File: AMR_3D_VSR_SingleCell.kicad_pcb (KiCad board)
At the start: 2 copper layers, 200.8 x 132.1 mm, 32 parts, among them P1 CONN_01X01, P2 CONN_01X01, P3 CONN_02X15, P4 CONN_02X05, P5 CONN_02X02, U1 AFF755b, U10 AFF755b, U11 AFF755b, U12 AFF755b, U13 AFF755b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

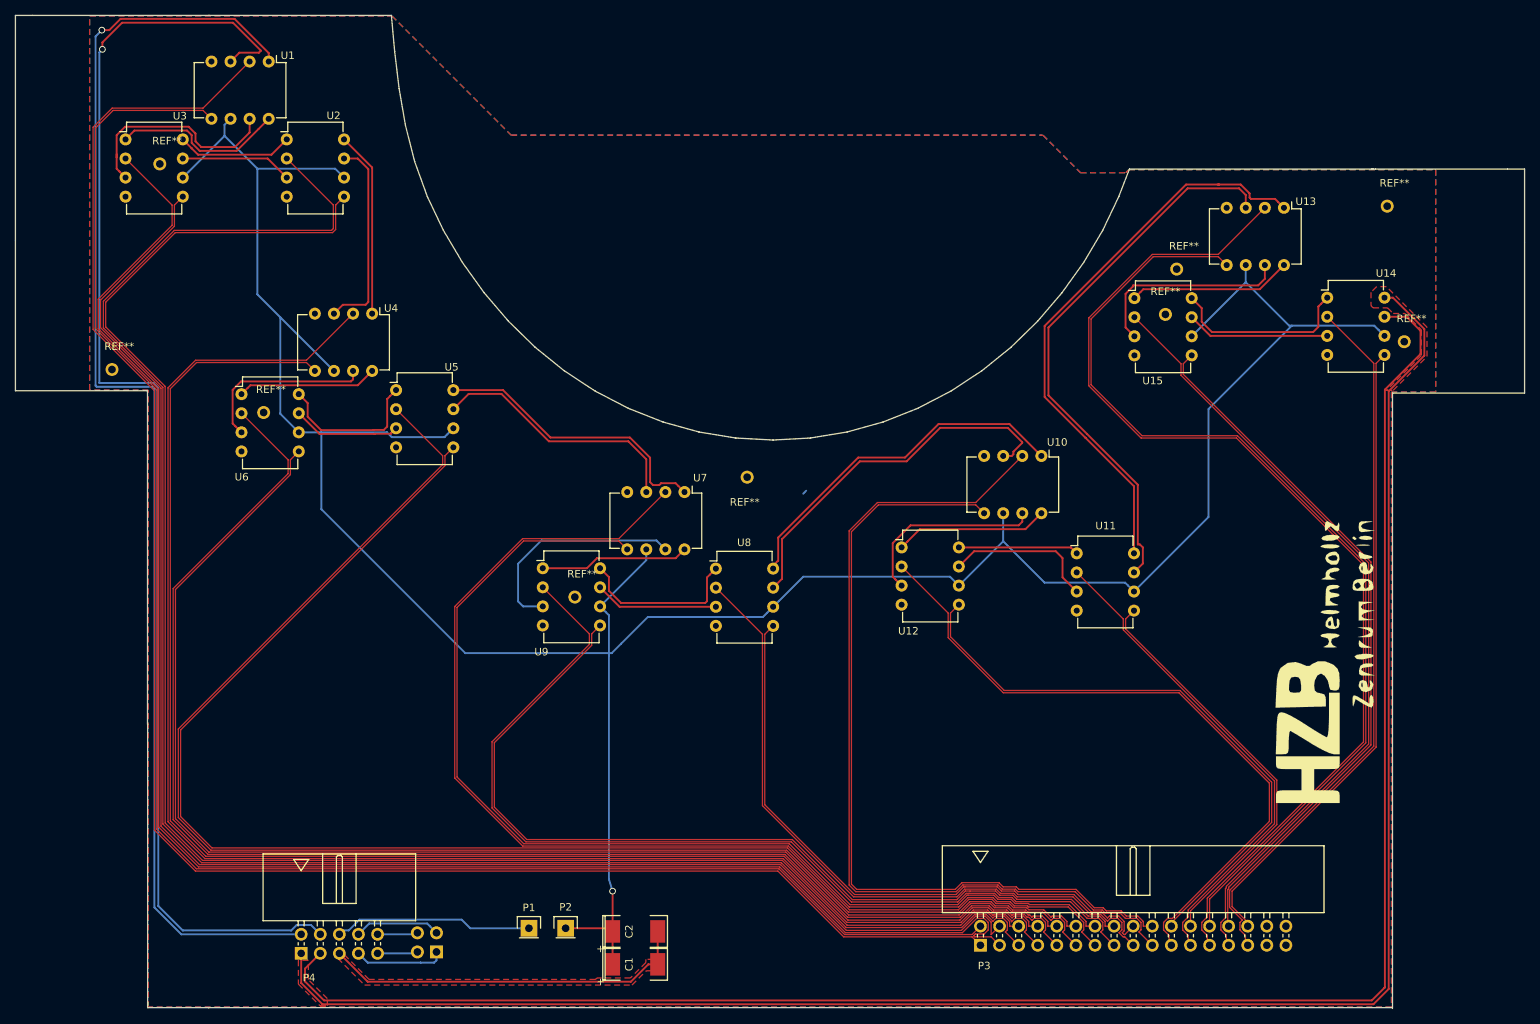
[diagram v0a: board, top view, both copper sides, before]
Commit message: Drillholes + additional load included.  Committer: Schmitz <ltu@basisit.de>  Changes to be committed: 	modified:   AMR_3D_VSR_SingleCell.kicad_pcb 	modified:   AMR_3D_VSR_SingleCell.kicad_pcb-bak
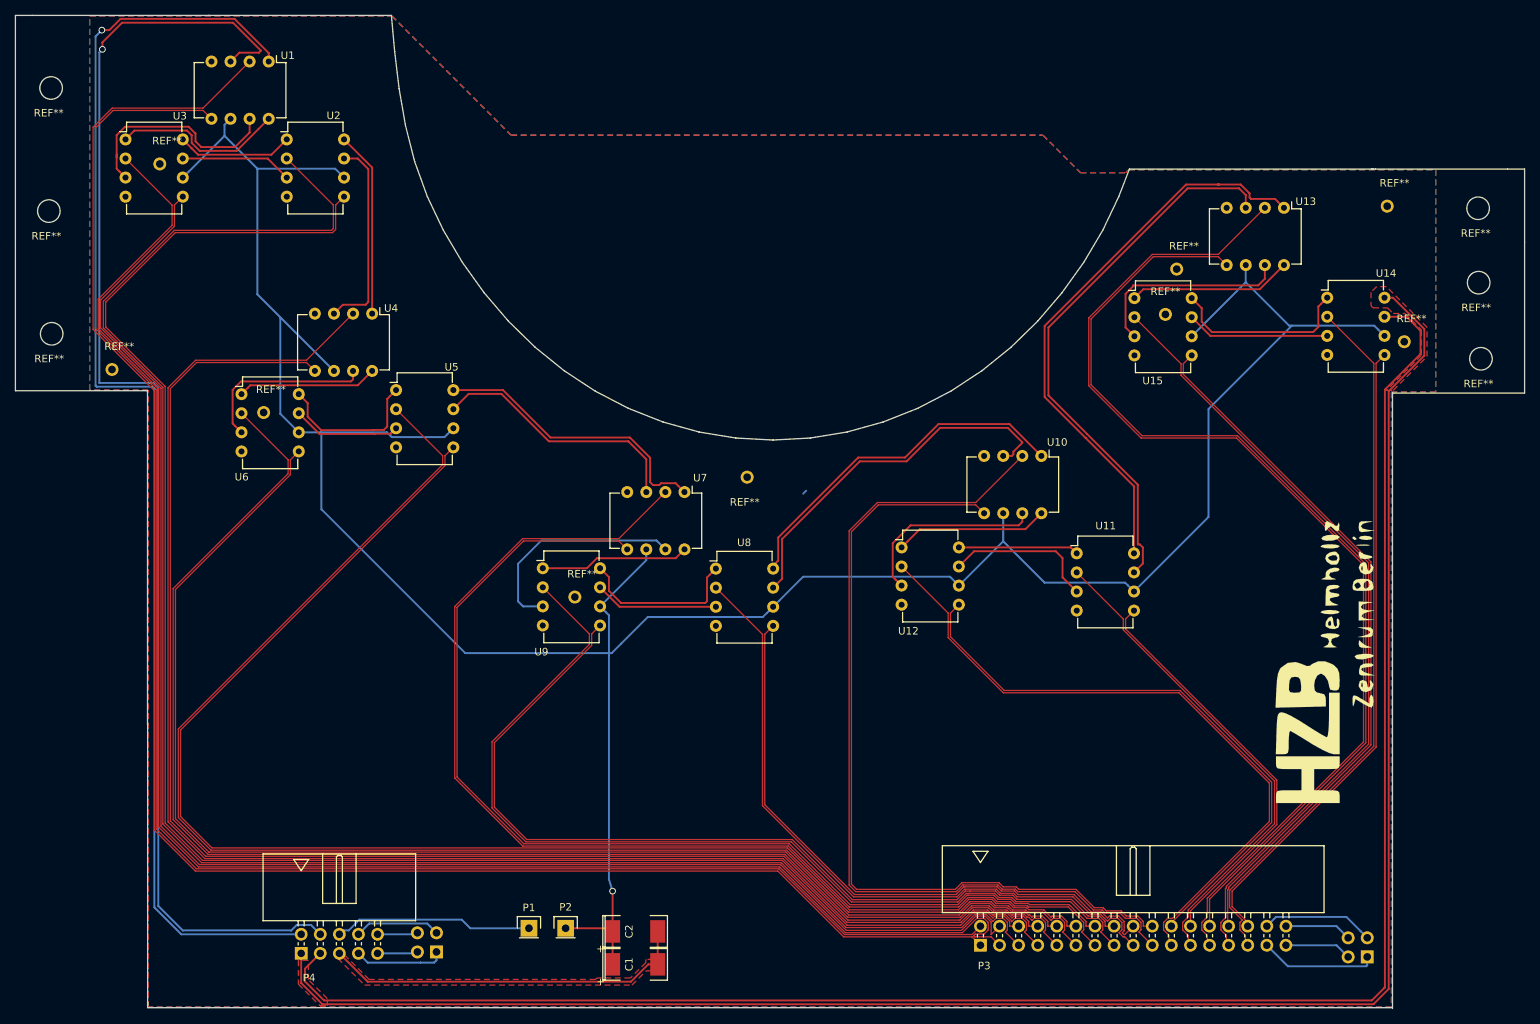
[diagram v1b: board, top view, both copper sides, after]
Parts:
- added P5: CONN_02X02, Pin_Headers:Pin_Header_Straight_2x02, B.Cu at (289.5, 206.2)
- added REF**: through hole, Connect:1pin, F.Cu at (304.6, 126.6)
- added REF**: through hole, Connect:1pin, F.Cu at (304.3, 116.5)
- added REF**: through hole, Connect:1pin, F.Cu at (304.2, 106.6)
- added REF**: through hole, Connect:1pin, F.Cu at (114.5, 123.3)
- added REF**: through hole, Connect:1pin, F.Cu at (114.1, 107.0)
- added REF**: through hole, Connect:1pin, F.Cu at (114.4, 90.6)
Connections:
- P3 pad 31: (no net) -> Load1
- P3 pad 32: (no net) -> Load3
- P3 pad 33: (no net) -> Load2
- P3 pad 34: (no net) -> Load4
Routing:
- net Load1: track 12.1 -> 27.8 mm
- net Load3: track 11.5 -> 26.5 mm
- net Load4: track 5.38 -> 14.3 mm
- net Load2: track 5.38 -> 14.3 mm
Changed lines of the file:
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@@
     (thickness 1.6)
     (drawings 60)
-    (tracks 839)
+    (tracks 851)
     (zones 0)
-    (modules 32)
+    (modules 39)
     (nets 69)
   )
   (page A3)
   (layers
-    (0 F.Cu signal)
-    (31 B.Cu signal hide)
+    (0 F.Cu signal hide)
+    (31 B.Cu signal)
     (32 B.Adhes user hide)
     (33 F.Adhes user hide)
@@
     (mod_text_size 1 1)
     (mod_text_width 0.15)
-    (pad_size 2.44 1.12)
-    (pad_drill 0)
+    (pad_size 1.7 1.7)
+    (pad_drill 1)
     (pad_to_mask_clearance 0)
     (aux_axis_origin 0 0)
@@
     (add_net U9+)
     (add_net U9-)
+  )
+  (module Pin_Headers:Pin_Header_Straight_2x02 (layer B.Cu)
+    (at 289.48 206.22 90)
+    (descr "Through hole pin header")
+    (tags "pin header")
+    (fp_text reference P5 (at 0 5.1 90) (layer B.SilkS)
+      (effects (font (size 1 1) (thickness 0.15)) (justify mirror))
+    )
+    (fp_text value CONN_02X02 (at 0 3.1 90) (layer B.Fab)
+      (effects (font (size 1 1) (thickness 0.15)) (justify mirror))
+    )
+    (fp_line (start -1.75 1.75) (end -1.75 -4.3) (layer B.CrtYd) (width 0.05))
+    (fp_line (start 4.3 1.75) (end 4.3 -4.3) (layer B.CrtYd) (width 0.05))
+    (fp_line (start -1.75 1.75) (end 4.3 1.75) (layer B.CrtYd) (width 0.05))
+    (fp_line (start -1.75 -4.3) (end 4.3 -4.3) (layer B.CrtYd) (width 0.05))
+    (fp_line (start -1.55 0) (end -1.55 1.55) (layer B.SilkS) (width 0.15))
+    (fp_line (start 0 1.55) (end -1.55 1.55) (layer B.SilkS) (width 0.15))
+    (fp_line (start -1.27 -1.27) (end 1.27 -1.27) (layer B.SilkS) (width 0.15))
+    (fp_line (start 1.27 -1.27) (end 1.27 1.27) (layer B.SilkS) (width 0.15))
+    (fp_line (start 1.27 1.27) (end 3.81 1.27) (layer B.SilkS) (width 0.15))
+    (fp_line (start 3.81 1.27) (end 3.81 -3.81) (layer B.SilkS) (width 0.15))
+    (fp_line (start 3.81 -3.81) (end -1.27 -3.81) (layer B.SilkS) (width 0.15))
+    (fp_line (start -1.27 -3.81) (end -1.27 -1.27) (layer B.SilkS) (width 0.15))
+    (pad 1 thru_hole rect (at 0 0 90) (size 1.7272 1.7272) (drill 1.016) (layers *.Cu *.Mask B.SilkS)
+      (net 65 Load1))
+    (pad 2 thru_hole oval (at 2.54 0 90) (size 1.7272 1.7272) (drill 1.016) (layers *.Cu *.Mask B.SilkS)
+      (net 66 Load3))
+    (pad 3 thru_hole oval (at 0 -2.54 90) (size 1.7272 1.7272) (drill 1.016) (layers *.Cu *.Mask B.SilkS)
+      (net 67 Load2))
+    (pad 4 thru_hole oval (at 2.54 -2.54 90) (size 1.7272 1.7272) (drill 1.016) (layers *.Cu *.Mask B.SilkS)
+      (net 68 Load4))
+    (model Pin_Headers.3dshapes/Pin_Header_Straight_2x02.wrl
+      (at (xyz 0.05 -0.05 0))
+      (scale (xyz 1 1 1))
+      (rotate (xyz 0 0 90))
+    )
+  )
+  (module Connect:1pin (layer F.Cu)
+    (at 304.605 126.645)
+    (descr "module 1 pin (ou trou mecanique de percage)")
+    (tags DEV)
+    (fp_text reference REF** (at -0.325 3.325) (layer F.SilkS)
+      (effects (font (size 1 1) (thickness 0.15)))
+    )
+    (fp_text value "through hole" (at 0 2.794) (layer F.Fab)
+      (effects (font (size 1 1) (thickness 0.15)))
+    )
+    (pad "" np_thru_hole circle (at 0 0) (size 3 3) (drill 3) (layers *.Cu *.Mask))
+  )
+  (module Connect:1pin (layer F.Cu)
+    (at 304.305 116.52)
+    (descr "module 1 pin (ou trou mecanique de percage)")
+    (tags DEV)
+    (fp_text reference REF** (at -0.325 3.325) (layer F.SilkS)
+      (effects (font (size 1 1) (thickness 0.15)))
+    )
+    (fp_text value "through hole" (at 0 2.794) (layer F.Fab)
+      (effects (font (size 1 1) (thickness 0.15)))
+    )
+    (pad "" np_thru_hole circle (at 0 0) (size 3 3) (drill 3) (layers *.Cu *.Mask))
+  )
+  (module Connect:1pin (layer F.Cu)
+    (at 304.23 106.62)
+    (descr "module 1 pin (ou trou mecanique de percage)")
+    (tags DEV)
+    (fp_text reference REF** (at -0.325 3.325) (layer F.SilkS)
+      (effects (font (size 1 1) (thickness 0.15)))
+    )
+    (fp_text value "through hole" (at 0 2.794) (layer F.Fab)
+      (effects (font (size 1 1) (thickness 0.15)))
+    )
+    (pad "" np_thru_hole circle (at 0 0) (size 3 3) (drill 3) (layers *.Cu *.Mask))
+  )
+  (module Connect:1pin (layer F.Cu)
+    (at 114.455 123.32)
+    (descr "module 1 pin (ou trou mecanique de percage)")
+    (tags DEV)
+    (fp_text reference REF** (at -0.325 3.325) (layer F.SilkS)
+      (effects (font (size 1 1) (thickness 0.15)))
+    )
+    (fp_text value "through hole" (at 0 2.794) (layer F.Fab)
+      (effects (font (size 1 1) (thickness 0.15)))
+    )
+    (pad "" np_thru_hole circle (at 0 0) (size 3 3) (drill 3) (layers *.Cu *.Mask))
+  )
+  (module Connect:1pin (layer F.Cu)
+    (at 114.08 106.995)
+    (descr "module 1 pin (ou trou mecanique de percage)")
+    (tags DEV)
+    (fp_text reference REF** (at -0.325 3.325) (layer F.SilkS)
+      (effects (font (size 1 1) (thickness 0.15)))
+    )
+    (fp_text value "through hole" (at 0 2.794) (layer F.Fab)
+      (effects (font (size 1 1) (thickness 0.15)))
+    )
+    (pad "" np_thru_hole circle (at 0 0) (size 3 3) (drill 3) (layers *.Cu *.Mask))
+  )
+  (module Connect:1pin (layer F.Cu)
+    (at 114.38 90.62)
+    (descr "module 1 pin (ou trou mecanique de percage)")
+    (tags DEV)
+    (fp_text reference REF** (at -0.325 3.325) (layer F.SilkS)
+      (effects (font (size 1 1) (thickness 0.15)))
+    )
+    (fp_text value "through hole" (at 0 2.794) (layer F.Fab)
+      (effects (font (size 1 1) (thickness 0.15)))
+    )
+    (pad "" np_thru_hole circle (at 0 0) (size 3 3) (drill 3) (layers *.Cu *.Mask))
   )
   (module Connect:1pin (layer F.Cu)
@@
     (pad 30 thru_hole circle (at 35.56 -2.54) (size 1.7 1.7) (drill 1) (layers *.Cu *.Mask F.SilkS)
       (net 25 U15+))
-    (pad 31 thru_hole circle (at 38.1 0) (size 1.7 1.7) (drill 1) (layers *.Cu *.Mask F.SilkS))
-    (pad 32 thru_hole circle (at 38.1 -2.54) (size 1.7 1.7) (drill 1) (layers *.Cu *.Mask F.SilkS))
-    (pad 33 thru_hole circle (at 40.64 0) (size 1.7 1.7) (drill 1) (layers *.Cu *.Mask F.SilkS))
-    (pad 34 thru_hole circle (at 40.64 -2.54) (size 1.7 1.7) (drill 1) (layers *.Cu *.Mask F.SilkS))
+    (pad 31 thru_hole circle (at 38.1 0) (size 1.7 1.7) (drill 1) (layers *.Cu *.Mask F.SilkS)
+      (net 65 Load1))
+    (pad 32 thru_hole circle (at 38.1 -2.54) (size 1.7 1.7) (drill 1) (layers *.Cu *.Mask F.SilkS)
+      (net 66 Load3))
+    (pad 33 thru_hole circle (at 40.64 0) (size 1.7 1.7) (drill 1) (layers *.Cu *.Mask F.SilkS)
+      (net 67 Load2))
+    (pad 34 thru_hole circle (at 40.64 -2.54) (size 1.7 1.7) (drill 1) (layers *.Cu *.Mask F.SilkS)
+      (net 68 Load4))
   )
   (module Connect:1pin (layer F.Cu)
@@
   (segment (start 291.82651 210.274896) (end 291.753246 210.34816) (width 0.254) (layer F.Cu) (net 64))
   (segment (start 148.15801 207.78199) (end 150.19 205.75) (width 0.254) (layer F.Cu) (net 64))
+  (segment (start 276.12 204.67) (end 278.914601 207.464601) (width 0.254) (layer B.Cu) (net 65))
+  (segment (start 278.914601 207.464601) (end 289.352999 207.464601) (width 0.254) (layer B.Cu) (net 65))
+  (segment (start 289.352999 207.464601) (end 289.48 207.3376) (width 0.254) (layer B.Cu) (net 65))
+  (segment (start 289.48 207.3376) (end 289.48 206.22) (width 0.254) (layer B.Cu) (net 65))
   (segment (start 155.27 205.75) (end 156.501001 206.981001) (width 0.254) (layer B.Cu) (net 65))
   (segment (start 156.501001 206.981001) (end 163.528209 206.981001) (width 0.254) (layer B.Cu) (net 65))
@@
   (segment (start 165.34722 206.97758) (end 165.64948 206.67532) (width 0.254) (layer B.Cu) (net 65))
   (segment (start 165.64948 206.67532) (end 165.64948 205.55772) (width 0.254) (layer B.Cu) (net 65))
+  (segment (start 276.12 202.13) (end 277.351001 200.898999) (width 0.254) (layer B.Cu) (net 66))
+  (segment (start 277.351001 200.898999) (end 286.698999 200.898999) (width 0.254) (layer B.Cu) (net 66))
+  (segment (start 286.698999 200.898999) (end 288.616401 202.816401) (width 0.254) (layer B.Cu) (net 66))
+  (segment (start 288.616401 202.816401) (end 289.48 203.68) (width 0.254) (layer B.Cu) (net 66))
   (segment (start 155.27 203.21) (end 156.706881 201.773119) (width 0.254) (layer B.Cu) (net 66))
   (segment (start 156.706881 201.773119) (end 164.404879 201.773119) (width 0.254) (layer B.Cu) (net 66))
   (segment (start 164.404879 201.773119) (end 164.785881 202.154121) (width 0.254) (layer B.Cu) (net 66))
   (segment (start 164.785881 202.154121) (end 165.64948 203.01772) (width 0.254) (layer B.Cu) (net 66))
+  (segment (start 278.66 204.67) (end 285.39 204.67) (width 0.254) (layer B.Cu) (net 67))
+  (segment (start 285.39 204.67) (end 286.94 206.22) (width 0.254) (layer B.Cu) (net 67))
   (segment (start 157.81 205.75) (end 162.9172 205.75) (width 0.254) (layer B.Cu) (net 67))
   (segment (start 162.9172 205.75) (end 163.10948 205.55772) (width 0.254) (layer B.Cu) (net 67))
+  (segment (start 278.66 202.13) (end 285.39 202.13) (width 0.254) (layer B.Cu) (net 68))
+  (segment (start 285.39 202.13) (end 286.94 203.68) (width 0.254) (layer B.Cu) (net 68))
   (segment (start 157.81 203.21) (end 162.9172 203.21) (width 0.254) (layer B.Cu) (net 68))
   (segment (start 162.9172 203.21) (end 163.10948 203.01772) (width 0.254) (layer B.Cu) (net 68))
